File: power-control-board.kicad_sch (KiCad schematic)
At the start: 25 parts, among them J1 Conn_01x02_Socket, J2 Raspberry_Pi_2_3, U2 XIAO-ESP32-C6-DIP

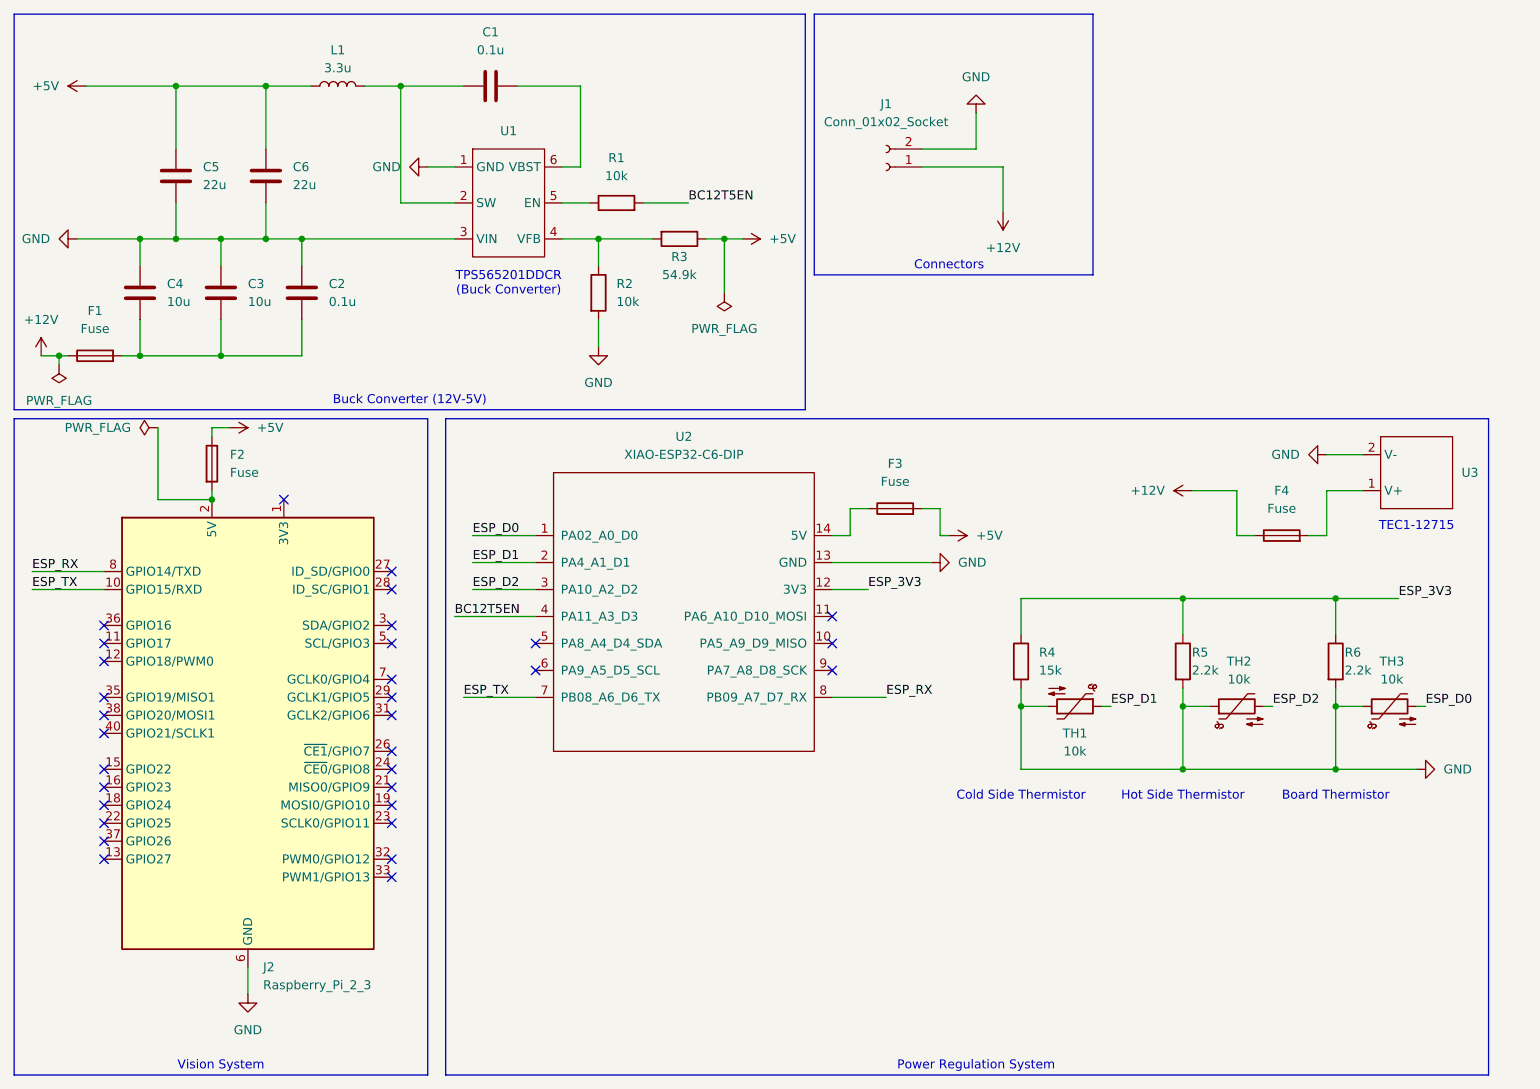
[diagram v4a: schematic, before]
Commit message: Added some footprints
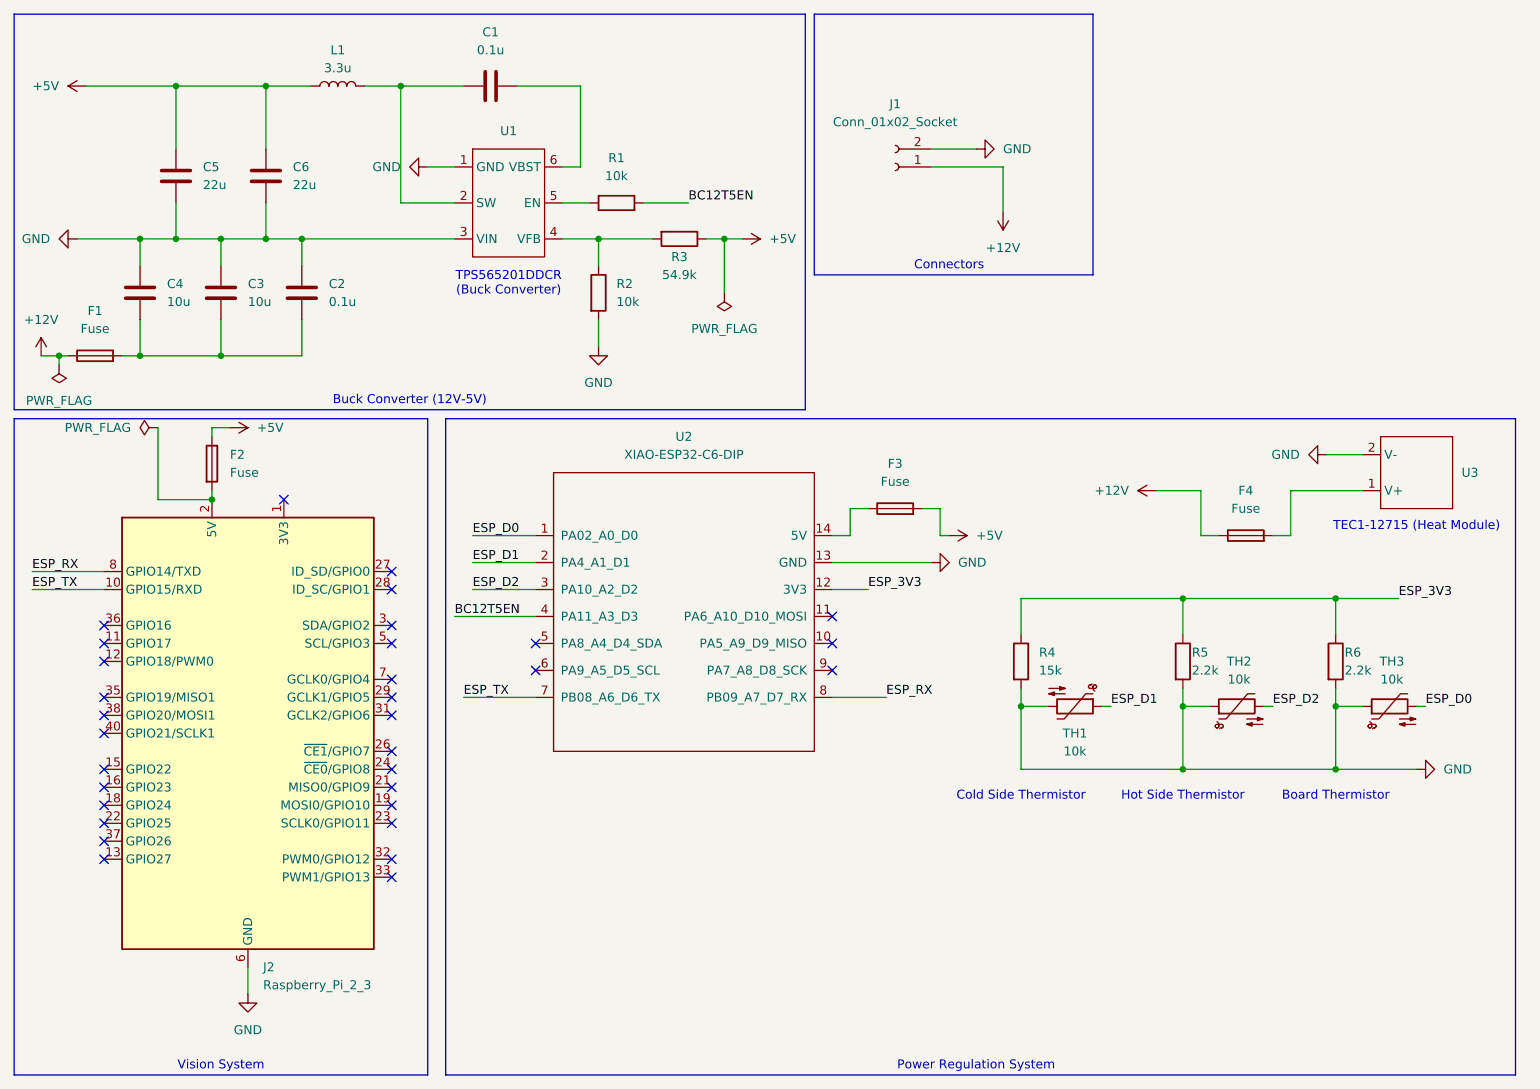
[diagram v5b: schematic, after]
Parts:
- F1, F2, F3, F4: footprint (none) -> Fuse:Fuseholder_Blade_Mini_Keystone_3568
- R1, R2, R3: footprint (none) -> Resistor_SMD:R_0201_0603Metric
- R4, R5, R6: footprint (none) -> Resistor_SMD:R_0402_1005Metric
- TH1, TH2, TH3: footprint (none) -> Connector_PinHeader_2.54mm:PinHeader_1x02_P2.54mm_Vertical
- U1: footprint (none) -> Package_TO_SOT_SMD:Texas_DDF0008A_SOT-8_1.6x2.9mm_P0.65mm
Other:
- note added: "TEC1-12715 (Heat Module)"
- note removed: "TEC1-12715"
- moved on the sheet: F4, J1
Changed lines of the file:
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@@
 	(rectangle
 		(start 74.93 71.12)
-		(end 222.25 163.83)
+		(end 226.06 163.83)
 		(stroke
 			(width 0)
@@
 		)
 	)
-	(text "TEC1-12715"
+	(text "TEC1-12715 (Heat Module)"
 		(exclude_from_sim no)
 		(at 212.09 86.36 0)
@@
 	(wire
 		(pts
-			(xy 142.24 33.02) (xy 149.86 33.02)
+			(xy 143.51 33.02) (xy 149.86 33.02)
 		)
 		(stroke
@@
 	(wire
 		(pts
-			(xy 186.69 87.63) (xy 189.23 87.63)
+			(xy 181.61 87.63) (xy 184.15 87.63)
 		)
 		(stroke
@@
 	(wire
 		(pts
-			(xy 186.69 87.63) (xy 186.69 81.28)
+			(xy 181.61 87.63) (xy 181.61 81.28)
 		)
 		(stroke
@@
 	(wire
 		(pts
-			(xy 186.69 81.28) (xy 180.34 81.28)
+			(xy 181.61 81.28) (xy 175.26 81.28)
 		)
 		(stroke
@@
 	(wire
 		(pts
-			(xy 142.24 35.56) (xy 153.67 35.56)
+			(xy 143.51 35.56) (xy 153.67 35.56)
 		)
 		(stroke
@@
 	(wire
 		(pts
-			(xy 196.85 87.63) (xy 199.39 87.63)
+			(xy 191.77 87.63) (xy 194.31 87.63)
 		)
 		(stroke
@@
 	(wire
 		(pts
-			(xy 149.86 27.94) (xy 149.86 33.02)
-		)
-		(stroke
-			(width 0)
-			(type default)
-		)
-	)
-	(wire
-		(pts
 			(xy 102.87 40.64) (xy 109.22 40.64)
 		)
@@
 	(wire
 		(pts
-			(xy 199.39 87.63) (xy 199.39 81.28)
+			(xy 194.31 87.63) (xy 194.31 81.28)
 		)
 		(stroke
@@
 	(wire
 		(pts
-			(xy 199.39 81.28) (xy 204.47 81.28)
+			(xy 194.31 81.28) (xy 204.47 81.28)
 		)
 		(stroke
@@
 	(symbol
 		(lib_id "Device:Fuse")
-		(at 193.04 87.63 90)
+		(at 187.96 87.63 90)
 		(unit 1)
 		(body_style 1)
@@
 		(fields_autoplaced yes)
 		(property "Reference" "F4"
-			(at 193.04 81.28 90)
+			(at 187.96 81.28 90)
 			(show_name no)
 			(do_not_autoplace no)
@@
 		)
 		(property "Value" "Fuse"
-			(at 193.04 83.82 90)
+			(at 187.96 83.82 90)
 			(show_name no)
 			(do_not_autoplace no)
@@
 			)
 		)
-		(property "Footprint" ""
-			(at 193.04 89.408 90)
+		(property "Footprint" "Fuse:Fuseholder_Blade_Mini_Keystone_3568"
+			(at 187.96 89.408 90)
 			(hide yes)
 			(show_name no)
@@
 		)
 		(property "Datasheet" ""
-			(at 193.04 87.63 0)
+			(at 187.96 87.63 0)
 			(hide yes)
 			(show_name no)
@@
 		)
 		(property "Description" "Fuse"
-			(at 193.04 87.63 0)
+			(at 187.96 87.63 0)
 			(hide yes)
 			(show_name no)
@@
 			)
 		)
-		(property "Footprint" ""
+		(property "Footprint" "Resistor_SMD:R_0201_0603Metric"
 			(at 99.06 42.418 90)
 			(hide yes)
@@
 			)
 		)
-		(property "Footprint" ""
+		(property "Footprint" "Connector_PinHeader_2.54mm:PinHeader_1x02_P2.54mm_Vertical"
 			(at 165.1 111.76 0)
 			(hide yes)
@@
 			)
 		)
-		(property "Footprint" ""
+		(property "Footprint" "Connector_PinHeader_2.54mm:PinHeader_1x02_P2.54mm_Vertical"
 			(at 185.42 111.76 0)
 			(hide yes)
@@
 			)
 		)
-		(property "Footprint" ""
+		(property "Footprint" "Resistor_SMD:R_0402_1005Metric"
 			(at 154.432 105.41 90)
 			(hide yes)
@@
 	(symbol
 		(lib_id "power:GND")
+		(at 149.86 33.02 90)
+		(unit 1)
+		(body_style 1)
+		(exclude_from_sim no)
+		(in_bom yes)
+		(on_board yes)
+		(in_pos_files yes)
+		(dnp no)
+		(fields_autoplaced yes)
+		(property "Reference" "#PWR01"
+			(at 156.21 33.02 0)
+			(hide yes)
+			(show_name no)
+			(do_not_autoplace no)
+			(effects
+				(font
+					(size 1.27 1.27)
+				)
+			)
+		)
+		(property "Value" "GND"
+			(at 153.67 33.0199 90)
+			(show_name no)
+			(do_not_autoplace no)
+			(effects
+				(font
+					(size 1.27 1.27)
+				)
+				(justify right)
+			)
+		)
+		(property "Footprint" ""
+			(at 149.86 33.02 0)
+			(hide yes)
+			(show_name no)
+			(do_not_autoplace no)
+			(effects
+				(font
+					(size 1.27 1.27)
+				)
+			)
+		)
+		(property "Datasheet" ""
+			(at 149.86 33.02 0)
+			(hide yes)
+			(show_name no)
+			(do_not_autoplace no)
+			(effects
+				(font
+					(size 1.27 1.27)
+				)
+			)
+		)
+		(property "Description" "Power symbol creates a global label with name \"GND\" , ground"
+			(at 149.86 33.02 0)
+			(hide yes)
+			(show_name no)
+			(do_not_autoplace no)
+			(effects
+				(font
+					(size 1.27 1.27)
+				)
+			)
+		)
+		(pin "1"
+		)
+		(instances
+			(project "power-control-board"
+				(path "/7d94012d-711e-4ac6-a37b-a02914d38462"
+					(reference "#PWR01")
+					(unit 1)
+				)
+			)
+		)
+	)
+	(symbol
+		(lib_id "power:GND")
 		(at 96.52 60.96 0)
 		(unit 1)
@@
 			)
 		)
-		(property "Footprint" ""
+		(property "Footprint" "Resistor_SMD:R_0402_1005Metric"
 			(at 198.882 105.41 90)
 			(hide yes)
@@
 			)
 		)
-		(property "Footprint" ""
+		(property "Footprint" "Package_TO_SOT_SMD:Texas_DDF0008A_SOT-8_1.6x2.9mm_P0.65mm"
 			(at 83.82 40.64 0)
 			(hide yes)
@@
 	(symbol
 		(lib_id "power:+12V")
-		(at 180.34 81.28 90)
+		(at 175.26 81.28 90)
 		(unit 1)
 		(body_style 1)
@@
 		(fields_autoplaced yes)
 		(property "Reference" "#PWR08"
-			(at 184.15 81.28 0)
+			(at 179.07 81.28 0)
 			(hide yes)
 			(show_name no)
@@
 		)
 		(property "Value" "+12V"
-			(at 176.53 81.2799 90)
+			(at 171.45 81.2799 90)
 			(show_name no)
 			(do_not_autoplace no)
@@
 		)
 		(property "Footprint" ""
-			(at 180.34 81.28 0)
+			(at 175.26 81.28 0)
 			(hide yes)
 			(show_name no)
@@
 		)
 		(property "Datasheet" ""
-			(at 180.34 81.28 0)
+			(at 175.26 81.28 0)
 			(hide yes)
 			(show_name no)
@@
 		)
 		(property "Description" "Power symbol creates a global label with name \"+12V\""
-			(at 180.34 81.28 0)
+			(at 175.26 81.28 0)
 			(hide yes)
 			(show_name no)
@@
 			)
 		)
-		(property "Footprint" ""
+		(property "Footprint" "Fuse:Fuseholder_Blade_Mini_Keystone_3568"
 			(at 25.4 64.008 90)
 			(hide yes)
@@
 	)
 	(symbol
-		(lib_id "power:GND")
-		(at 149.86 27.94 180)
-		(unit 1)
-		(body_style 1)
-		(exclude_from_sim no)
-		(in_bom yes)
-		(on_board yes)
-		(in_pos_files yes)
-		(dnp no)
-		(fields_autoplaced yes)
-		(property "Reference" "#PWR01"
-			(at 149.86 21.59 0)
-			(hide yes)
-			(show_name no)
-			(do_not_autoplace no)
-			(effects
-				(font
-					(size 1.27 1.27)
-				)
-			)
-		)
-		(property "Value" "GND"
-			(at 149.86 22.86 0)
-			(show_name no)
-			(do_not_autoplace no)
-			(effects
-				(font
-					(size 1.27 1.27)
-				)
-			)
-		)
-		(property "Footprint" ""
-			(at 149.86 27.94 0)
-			(hide yes)
-			(show_name no)
-			(do_not_autoplace no)
-			(effects
-				(font
-					(size 1.27 1.27)
-				)
-			)
-		)
-		(property "Datasheet" ""
-			(at 149.86 27.94 0)
-			(hide yes)
-			(show_name no)
-			(do_not_autoplace no)
-			(effects
-				(font
-					(size 1.27 1.27)
-				)
-			)
-		)
-		(property "Description" "Power symbol creates a global label with name \"GND\" , ground"
-			(at 149.86 27.94 0)
-			(hide yes)
-			(show_name no)
-			(do_not_autoplace no)
-			(effects
-				(font
-					(size 1.27 1.27)
-				)
-			)
-		)
-		(pin "1"
-		)
-		(instances
-			(project "power-control-board"
-				(path "/7d94012d-711e-4ac6-a37b-a02914d38462"
-					(reference "#PWR01")
-					(unit 1)
-				)
-			)
-		)
-	)
-	(symbol
 		(lib_id "Device:R")
 		(at 96.52 53.34 0)
@@
 			)
 		)
-		(property "Footprint" ""
+		(property "Footprint" "Resistor_SMD:R_0201_0603Metric"
 			(at 94.742 53.34 90)
 			(hide yes)
@@
 			)
 		)
-		(property "Footprint" ""
+		(property "Footprint" "Resistor_SMD:R_0201_0603Metric"
 			(at 107.95 43.942 90)
 			(hide yes)
@@
 			)
 		)
-		(property "Footprint" ""
+		(property "Footprint" "Fuse:Fuseholder_Blade_Mini_Keystone_3568"
 			(at 40.132 77.47 90)
 			(hide yes)
@@
 			)
 		)
-		(property "Footprint" ""
+		(property "Footprint" "Connector_PinHeader_2.54mm:PinHeader_1x02_P2.54mm_Vertical"
 			(at 207.01 111.76 0)
 			(hide yes)
@@
 	(symbol
 		(lib_id "Connector:Conn_01x02_Socket")
-		(at 137.16 35.56 180)
+		(at 138.43 35.56 180)
 		(unit 1)
 		(body_style 1)
@@
 		(dnp no)
 		(property "Reference" "J1"
-			(at 137.16 26.67 0)
+			(at 138.43 26.67 0)
 			(show_name no)
 			(do_not_autoplace no)
@@
 		)
 		(property "Value" "Conn_01x02_Socket"
-			(at 137.16 29.21 0)
+			(at 138.43 29.21 0)
 			(show_name no)
 			(do_not_autoplace no)
@@
 		)
 		(property "Footprint" ""
-			(at 137.16 35.56 0)
+			(at 138.43 35.56 0)
 			(hide yes)
 			(show_name no)
@@
 		)
 		(property "Datasheet" ""
-			(at 137.16 35.56 0)
+			(at 138.43 35.56 0)
 			(hide yes)
 			(show_name no)
@@
 		)
 		(property "Description" "Generic connector, single row, 01x02, script generated"
-			(at 137.16 35.56 0)
+			(at 138.43 35.56 0)
 			(hide yes)
 			(show_name no)
@@
 			)
 		)
-		(property "Footprint" ""
+		(property "Footprint" "Fuse:Fuseholder_Blade_Mini_Keystone_3568"
 			(at 138.43 85.598 90)
 			(hide yes)
@@
 			)
 		)
-		(property "Footprint" ""
+		(property "Footprint" "Resistor_SMD:R_0402_1005Metric"
 			(at 177.292 105.41 90)
 			(hide yes)
